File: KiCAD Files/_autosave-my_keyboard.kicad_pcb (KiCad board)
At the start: 2 copper layers, 120 x 120 mm, 47 parts, among them K1 KEYSW, K10 KEYSW, K11 KEYSW, K12 KEYSW, K13 KEYSW, K14 KEYSW, K15 KEYSW, K16 KEYSW, K17 KEYSW, K2 KEYSW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

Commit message: Added KiCAD Library
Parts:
- D1, D10, D11, D12, D13, D14, D15, D16, D17, D18, D19, D2, D20, D3, D4, D5, D6, D7, D8, D9: moved to B.Cu
- turned D15 to 90 degrees
- turned D19 to 90 degrees
- turned D20 to 90 degrees

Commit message: Updated KiCAD Lib
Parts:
- moved H2 43.8 mm to (64.6, 103.3)
- moved H1 31.0 mm to (64.6, 93.2)
- moved H4 30.7 mm to (74.8, 103.3)
- moved H3 21.0 mm to (74.8, 93.2)

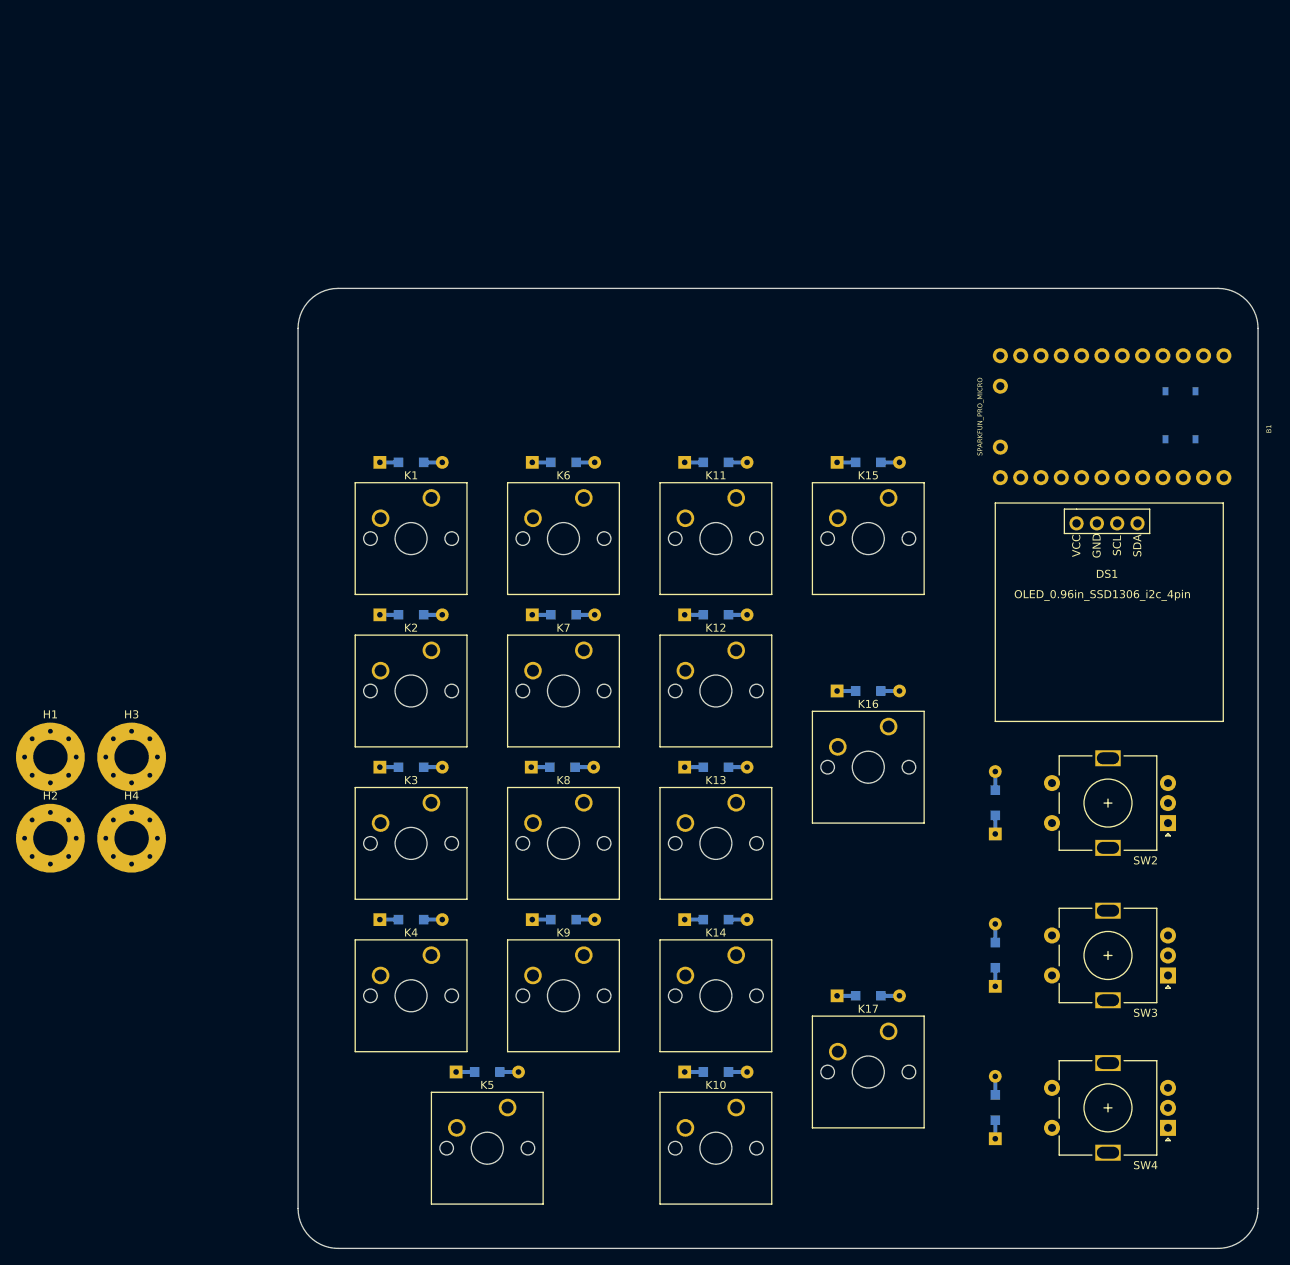
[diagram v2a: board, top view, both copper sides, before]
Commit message: Fixed Diode Issue
Previously used wrong diode symbol meant for simulation not design.
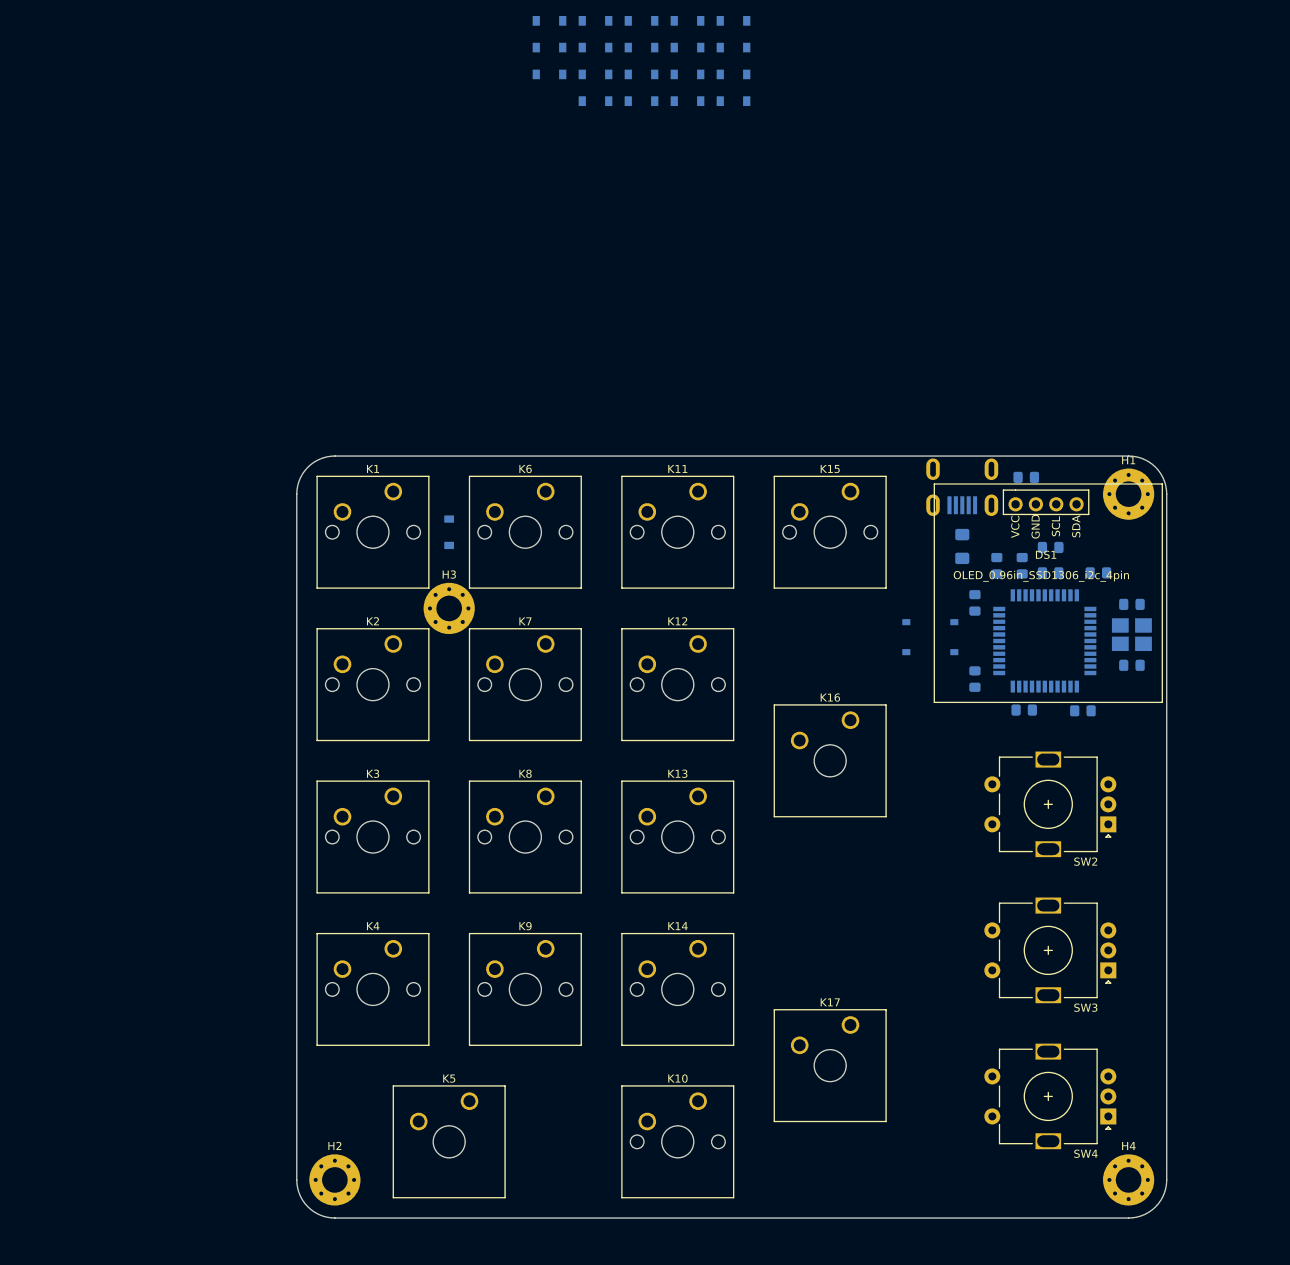
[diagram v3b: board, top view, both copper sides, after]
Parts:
- removed B1: SPARKFUN_PRO_MICRO, SparkFun:SPARKFUN_PRO_MICRO
- added C1: 22pF, Capacitor_SMD:C_0805_2012Metric_Pad1.15x1.40mm_HandSolder, B.Cu at (199.8, 74.1)
- added C2: 22pF, Capacitor_SMD:C_0805_2012Metric_Pad1.15x1.40mm_HandSolder, B.Cu at (199.8, 81.7)
- added C3: 0.1uF, Capacitor_SMD:C_0805_2012Metric_Pad1.15x1.40mm_HandSolder, B.Cu at (193.7, 87.4)
- added C4: 0.1uF, Capacitor_SMD:C_0805_2012Metric_Pad1.15x1.40mm_HandSolder, B.Cu at (180.2, 83.4)
- added C5: 0.1uF, Capacitor_SMD:C_0805_2012Metric_Pad1.15x1.40mm_HandSolder, B.Cu at (180.2, 73.9)
- added C6: 1uF, Capacitor_SMD:C_0805_2012Metric_Pad1.15x1.40mm_HandSolder, B.Cu at (189.6, 70.2)
- added C7: 0.1uF, Capacitor_SMD:C_0805_2012Metric_Pad1.15x1.40mm_HandSolder, B.Cu at (189.6, 67.0)
- added C8: 10uF, Capacitor_SMD:C_0805_2012Metric_Pad1.15x1.40mm_HandSolder, B.Cu at (186.6, 58.2)
- added F1: 500 mA, Fuse:Fuse_1206_3216Metric_Pad1.42x1.75mm_HandSolder, B.Cu at (178.6, 66.9)
- added J1: USB_B_Mini, random-keyboard-parts:Molex-0548190589, B.Cu at (178.6, 57.2)
- added R1: 22, Resistor_SMD:R_0805_2012Metric_Pad1.15x1.40mm_HandSolder, B.Cu at (186.1, 69.3)
- added R2: 22, Resistor_SMD:R_0805_2012Metric_Pad1.15x1.40mm_HandSolder, B.Cu at (182.9, 69.3)
- added R3: 10k, Resistor_SMD:R_0805_2012Metric_Pad1.15x1.40mm_HandSolder, B.Cu at (195.6, 70.2)
- added R4: 10k, Resistor_SMD:R_0805_2012Metric_Pad1.15x1.40mm_HandSolder, B.Cu at (186.3, 87.3)
- added U1: ATmega32U4-AU, Package_QFP:TQFP-44_10x10mm_P0.8mm, B.Cu at (188.9, 78.7)
- added Y1: 16MHz, Crystal:Crystal_SMD_3225-4Pin_3.2x2.5mm_HandSoldering, B.Cu at (199.8, 77.9)
- D1, D10, D11, D12, D13, D14, D15, D16, D17, D18, D19, D2, D20, D3, D4, D5, D6, D7, D8, D9: value DIODE -> D; footprint keyboard_parts:D_SOD123_axial -> Diode_SMD:D_SOD-123
- H1, H2, H3, H4: footprint MountingHole:MountingHole_4.3mm_M4_Pad_Via -> MountingHole:MountingHole_3.2mm_M3_Pad_Via
- K16, K17: footprint Button_Switch_Keyboard:SW_Cherry_MX_1.00u_PCB -> Button_Switch_Keyboard:SW_Cherry_MX_2.00u_Vertical_Plate
- K5: footprint Button_Switch_Keyboard:SW_Cherry_MX_1.00u_PCB -> Button_Switch_Keyboard:SW_Cherry_MX_2.00u_Plate
- moved D20 139.7 mm to (150.0, 1.16), turned to 0 degrees
- moved H1 138.7 mm to (199.4, 60.3)
- moved H4 131.7 mm to (199.4, 146.0)
- moved D5 125.4 mm to (132.7, 7.86)
- moved D15 124.9 mm to (138.5, 1.16), turned to 0 degrees
- moved D18 124.0 mm to (144.2, 1.16)
- moved D10 121.4 mm to (144.2, 11.2)
- moved D4 110.4 mm to (127.0, 4.51)
- moved D9 106.1 mm to (138.5, 7.86)
- moved D14 102.3 mm to (150.0, 11.2)
- moved D19 99.9 mm to (150.0, 4.51), turned to 0 degrees
- moved D8 90.0 mm to (132.7, 4.51)
- moved D13 86.7 mm to (144.2, 7.86)
- moved D3 86.4 mm to (132.7, 11.2)
- moved D17 78.9 mm to (150.0, 7.86)
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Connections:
- D1 pad 1: Net-(D1-Pad1) -> /row0
- D1 pad 2: /row0 -> Net-(D1-Pad2)
- D10 pad 1: Net-(D10-Pad1) -> /row4
- D10 pad 2: /row4 -> Net-(D10-Pad2)
- D11 pad 1: Net-(D11-Pad1) -> /row0
- D11 pad 2: /row0 -> Net-(D11-Pad2)
- D12 pad 1: Net-(D12-Pad1) -> /row1
- D12 pad 2: /row1 -> Net-(D12-Pad2)
- D13 pad 1: Net-(D13-Pad1) -> /row2
- D13 pad 2: /col2 -> Net-(D13-Pad2)
- D14 pad 1: Net-(D14-Pad1) -> /row3
- D14 pad 2: /row3 -> Net-(D14-Pad2)
- D15 pad 1: /encoder_S2B -> /row4
- D15 pad 2: /row4 -> /encoder_S2B
- D16 pad 1: Net-(D16-Pad1) -> /row0
- D16 pad 2: /row0 -> Net-(D16-Pad2)
- D17 pad 1: Net-(D17-Pad1) -> /row1
- D17 pad 2: /row1 -> Net-(D17-Pad2)
- D18 pad 1: Net-(D18-Pad1) -> /row2
- D18 pad 2: /col2 -> Net-(D18-Pad2)
- D19 pad 1: /encoder_S1B -> /row3
- D19 pad 2: /row3 -> /encoder_S1B
- D2 pad 1: Net-(D2-Pad1) -> /row1
- D2 pad 2: /row1 -> Net-(D2-Pad2)
- D20 pad 1: /encoder_S3B -> /row4
- D20 pad 2: /row4 -> /encoder_S3B
- D3 pad 1: Net-(D3-Pad1) -> /row2
- D3 pad 2: /col2 -> Net-(D3-Pad2)
- D4 pad 1: Net-(D4-Pad1) -> /row3
- D4 pad 2: /row3 -> Net-(D4-Pad2)
- D5 pad 1: Net-(D5-Pad1) -> /row4
- D5 pad 2: /row4 -> Net-(D5-Pad2)
- D6 pad 1: Net-(D6-Pad1) -> /row0
- D6 pad 2: /row0 -> Net-(D6-Pad2)
- D7 pad 1: Net-(D7-Pad1) -> /row1
- D7 pad 2: /row1 -> Net-(D7-Pad2)
- D8 pad 1: Net-(D8-Pad1) -> /row2
- D8 pad 2: /col2 -> Net-(D8-Pad2)
- D9 pad 1: Net-(D9-Pad1) -> /row3
- D9 pad 2: /row3 -> Net-(D9-Pad2)
- DS1 pad 1: VCC -> +5V
- K1 pad 2: Net-(D1-Pad1) -> Net-(D1-Pad2)
- K10 pad 2: Net-(D10-Pad1) -> Net-(D10-Pad2)
- K11 pad 2: Net-(D11-Pad1) -> Net-(D11-Pad2)
- K12 pad 2: Net-(D12-Pad1) -> Net-(D12-Pad2)
- K13 pad 2: Net-(D13-Pad1) -> Net-(D13-Pad2)
- K14 pad 2: Net-(D14-Pad1) -> Net-(D14-Pad2)
- K15 pad 2: Net-(D16-Pad1) -> Net-(D16-Pad2)
- K16 pad 2: Net-(D17-Pad1) -> Net-(D17-Pad2)
- K17 pad 2: Net-(D18-Pad1) -> Net-(D18-Pad2)
- K2 pad 2: Net-(D2-Pad1) -> Net-(D2-Pad2)
- K3 pad 2: Net-(D3-Pad1) -> Net-(D3-Pad2)
- K4 pad 2: Net-(D4-Pad1) -> Net-(D4-Pad2)
- K5 pad 2: Net-(D5-Pad1) -> Net-(D5-Pad2)
- K6 pad 2: Net-(D6-Pad1) -> Net-(D6-Pad2)
- K7 pad 2: Net-(D7-Pad1) -> Net-(D7-Pad2)
- K8 pad 2: Net-(D8-Pad1) -> Net-(D8-Pad2)
- K9 pad 2: Net-(D9-Pad1) -> Net-(D9-Pad2)
- SW1 pad 1: /RESET_SW -> GND
- SW1 pad 2: GND -> Net-(R3-Pad2)
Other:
- board size 120 x 120 mm -> 108.7 x 95.3 mm
- net class Default: trace_width 0.25 -> 0.254
- net class POWER added: clearance 0.2, trace_width 0.381, via_dia 0.8, via_drill 0.4
